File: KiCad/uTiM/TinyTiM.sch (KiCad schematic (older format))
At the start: 6 parts, among them P1 Data_In_Serial, P2 Data_Out_Serial, P5 Data_In_Serial, P6 Data_Out_Serial

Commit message: microTiM aka uTiM work in progress
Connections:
- net DI_A: now also P5.3 (P3); no longer P5.1 (P1)
- net GND: now also P5.1 (P1); no longer P5.3 (P3)
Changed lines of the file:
@@
 01 31 04 0B 88 21 58 40 0C C1 02 62 08 16 10 43 B0 80 18 82 05 C4 10 2C 20 86 60 01 31 04 0B 88
 21 58 40 0C C1 02 62 08 16 10 43 B0 80 18 82 05 C4 10 2C 20 86 60 01 31 04 0B 88 21 58 40 0C C1
-02 62 7C 03 3D 79 5E 0E 30 13 47 E7 00 00 00 00 49 45 4E 44 AE 42 60 82 81
+02 62 7C 03 3D 79 5E 0E 30 13 47 E7 00 00 00 00 49 45 4E 44 AE 42 60 82 E0
 EndData
 $EndBitmap
@@
 C1 ED 35 72 E0 F7 FB FF F1 1F FF F1 9F FF F9 9F C7 C7 C7 73 1A 9F 2B 70 38 1C FB F6 ED 3B 79 F2
 E4 23 8F 3C 52 B0 F1 D9 2E 76 F1 FF 03 17 ED 19 47 28 92 59 FB 00 00 00 00 49 45 4E 44 AE 42 60
-82 3D
+82 6C
 EndData
 $EndBitmap
@@
 F2 "GND" I L 8000 2000 60
 F3 "5V" I R 10050 2000 60
-F4 "DO_G" O R 10050 1700 60
+F4 "DI_H" O R 10050 1700 60
 F5 "DI_G" I L 8000 1700 60
-F6 "CO_G" O R 10050 1850 60
+F6 "CI_H" O R 10050 1850 60
 F7 "CI_G" I L 8000 1850 60
 $EndSheet
@@
 F2 "GND" I L 8000 2750 60
 F3 "5V" I R 10050 2750 60
-F4 "DO_F" O R 10050 2450 60
+F4 "DI_G" O R 10050 2450 60
 F5 "DI_F" I L 8000 2450 60
-F6 "CO_F" O R 10050 2600 60
+F6 "CI_G" O R 10050 2600 60
 F7 "CI_F" I L 8000 2600 60
 $EndSheet
@@
 F2 "GND" I L 8000 3500 60
 F3 "5V" I R 10050 3500 60
-F4 "DO_E" O R 10050 3200 60
+F4 "DI_F" O R 10050 3200 60
 F5 "DI_E" I L 8000 3200 60
-F6 "CO_E" O R 10050 3350 60
+F6 "CI_F" O R 10050 3350 60
 F7 "CI_E" I L 8000 3350 60
 $EndSheet
@@
 F2 "GND" I L 8000 4250 60
 F3 "5V" I R 10050 4250 60
-F4 "DO_D" O R 10050 3950 60
-F5 "DI_D" I L 8000 3950 60
-F6 "CO_D" O R 10050 4100 60
-F7 "CI_D" I L 8000 4100 60
+F4 "DI_D" I L 8000 3950 60
+F5 "CI_D" I L 8000 4100 60
+F6 "CI_E" O R 10050 4100 60
+F7 "DI_E" O R 10050 3950 60
 $EndSheet
 $Sheet
@@
 F2 "GND" I L 8000 5000 60
 F3 "5V" I R 10050 5000 60
-F4 "DO_C" O R 10050 4700 60
-F5 "DI_C" I L 8000 4700 60
-F6 "CO_C" O R 10050 4850 60
-F7 "CI_C" I L 8000 4850 60
+F4 "DI_C" I L 8000 4700 60
+F5 "CI_C" I L 8000 4850 60
+F6 "CI_D" O R 10050 4850 60
+F7 "DI_D" O R 10050 4700 60
 $EndSheet
 $Sheet
@@
 F2 "GND" I L 8000 5750 60
 F3 "5V" I R 10050 5750 60
-F4 "DO_B" O R 10050 5450 60
-F5 "DI_B" I L 8000 5450 60
-F6 "CO_B" O R 10050 5600 60
-F7 "CI_B" I L 8000 5600 60
+F4 "DI_B" I L 8000 5450 60
+F5 "CI_B" I L 8000 5600 60
+F6 "CI_C" O R 10050 5600 60
+F7 "DI_C" O R 10050 5450 60
 $EndSheet
 $Sheet
@@
 F0 "Row_A" 40
 F1 "Row_A.sch" 40
-F2 "DO_A" O R 10050 6200 60
-F3 "GND" I L 8000 6500 60
-F4 "DI_A" I L 8000 6200 60
-F5 "5V" I R 10050 6500 60
-F6 "CO_A" O R 10050 6350 60
-F7 "CI_A" I L 8000 6350 60
+F2 "GND" I L 8000 6500 60
+F3 "DI_A" I L 8000 6200 60
+F4 "5V" I R 10050 6500 60
+F5 "CI_A" I L 8000 6350 60
+F6 "CI_B" O R 10050 6350 60
+F7 "DI_B" O R 10050 6200 60
 $EndSheet
 $Comp
@@
 Text Label 10600 2000 2    60   ~ 0
 5V
-Text Label 10600 1700 2    60   ~ 0
-DO_G
 Wire Wire Line
 	10600 2000 10050 2000
 Wire Wire Line
 	10600 1850 10050 1850
-Text Label 10600 1850 2    60   ~ 0
-CO_G
 Wire Wire Line
 	10050 2450 10600 2450
 Text Label 10600 2750 2    60   ~ 0
 5V
-Text Label 10600 2450 2    60   ~ 0
-DO_F
 Wire Wire Line
 	10600 2750 10050 2750
 Wire Wire Line
 	10600 2600 10050 2600
-Text Label 10600 2600 2    60   ~ 0
-CO_F
 Wire Wire Line
 	10050 3200 10600 3200
 Text Label 10600 3500 2    60   ~ 0
 5V
-Text Label 10600 3200 2    60   ~ 0
-DO_E
 Wire Wire Line
 	10600 3500 10050 3500
 Wire Wire Line
 	10600 3350 10050 3350
-Text Label 10600 3350 2    60   ~ 0
-CO_E
 Wire Wire Line
 	10050 3950 10600 3950
 Text Label 10600 4250 2    60   ~ 0
 5V
-Text Label 10600 3950 2    60   ~ 0
-DO_D
 Wire Wire Line
 	10600 4250 10050 4250
 Wire Wire Line
 	10600 4100 10050 4100
-Text Label 10600 4100 2    60   ~ 0
-CO_D
 Wire Wire Line
 	10050 4700 10600 4700
 Text Label 10600 5000 2    60   ~ 0
 5V
-Text Label 10600 4700 2    60   ~ 0
-DO_C
 Wire Wire Line
 	10600 5000 10050 5000
 Wire Wire Line
 	10600 4850 10050 4850
-Text Label 10600 4850 2    60   ~ 0
-CO_C
 Wire Wire Line
 	10050 5450 10600 5450
@@
 5V
 Text Label 10600 5450 2    60   ~ 0
-DO_B
+DI_C
 Wire Wire Line
 	10600 5750 10050 5750
@@
 	10600 5600 10050 5600
 Text Label 10600 5600 2    60   ~ 0
-CO_B
+CI_C
 Wire Wire Line
 	10050 6200 10600 6200
 Text Label 10600 6500 2    60   ~ 0
 5V
-Text Label 10600 6200 2    60   ~ 0
-DO_A
 Wire Wire Line
 	10600 6500 10050 6500
 Wire Wire Line
 	10600 6350 10050 6350
-Text Label 10600 6350 2    60   ~ 0
-CO_A
 Wire Wire Line
 	2800 1450 3050 1450
@@
 F 6 "0.1\"" H 1350 2575 60  0001 L CNN "Field6"
 	1    1350 2325
-	-1   0    0    -1
+	-1   0    0    1
 $EndComp
 $Comp
@@
 	1    0    0    -1
 $EndComp
+Text Label 10600 6200 2    60   ~ 0
+DI_B
+Text Label 10600 6350 2    60   ~ 0
+CI_B
+Text Label 10600 4700 2    60   ~ 0
+DI_D
+Text Label 10600 4850 2    60   ~ 0
+CI_D
+Text Label 10600 3950 2    60   ~ 0
+DI_E
+Text Label 10600 4100 2    60   ~ 0
+CI_E
+Text Label 10600 3200 2    60   ~ 0
+DI_F
+Text Label 10600 3350 2    60   ~ 0
+CI_F
+Text Label 10600 2450 2    60   ~ 0
+DI_G
+Text Label 10600 2600 2    60   ~ 0
+CI_G
+Text Label 10600 1700 2    60   ~ 0
+DI_H
+Text Label 10600 1850 2    60   ~ 0
+CI_H
 $EndSCHEMATC

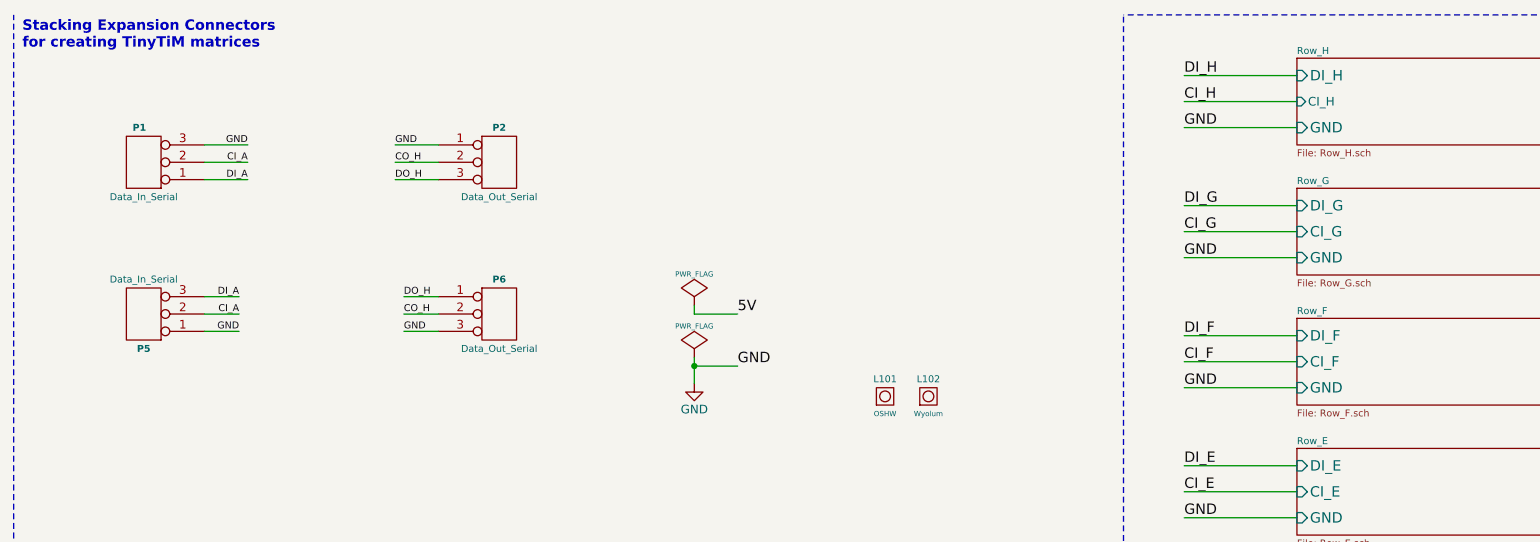
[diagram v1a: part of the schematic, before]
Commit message: work in progress, microTIM using APA102
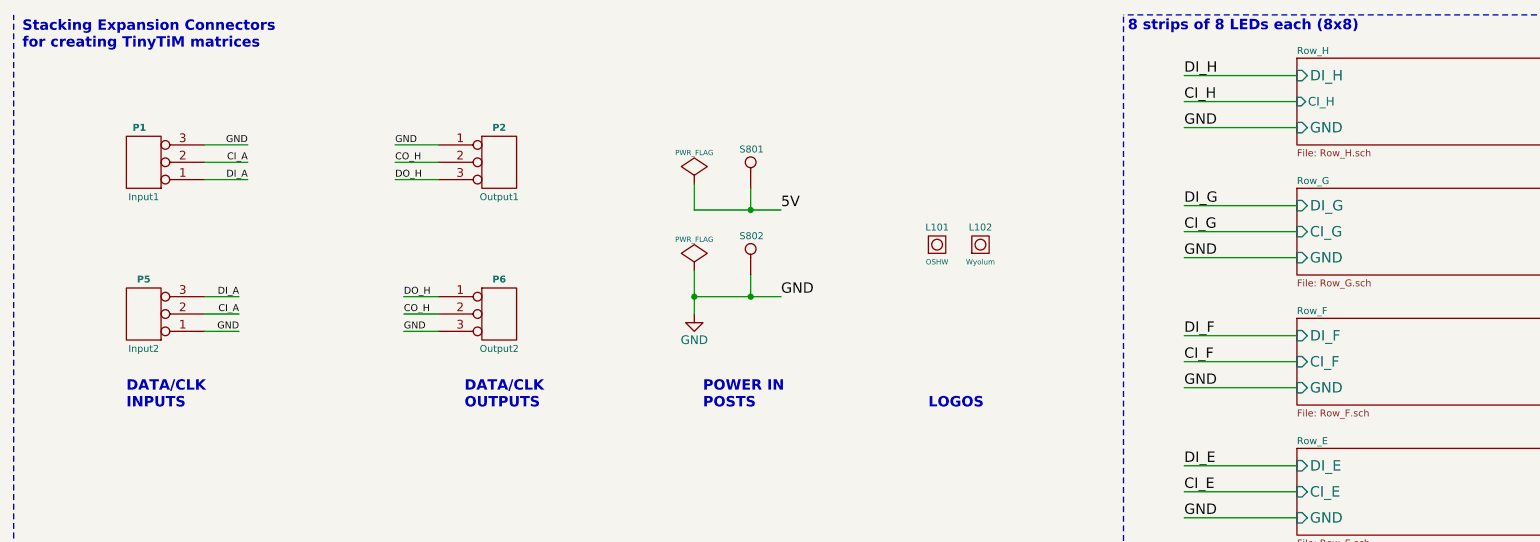
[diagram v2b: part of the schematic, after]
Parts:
- added S801: 5V, symbol CONN_1
- added S802: GND, symbol CONN_1
- P1: value Data_In_Serial -> Input1; footprint TinyTiM_Libs:Conn_x3_PTSM -> TinyTiM_Libs:JST_3pin_SRSS
- P2: value Data_Out_Serial -> Output1; footprint TinyTiM_Libs:Conn_x3_PTSM -> TinyTiM_Libs:JST_3pin_SRSS
- P5: value Data_In_Serial -> Input2; footprint TinyTiM_Libs:Conn_x3_PTSM -> TinyTiM_Libs:JST_3pin_SRSS
- P6: value Data_Out_Serial -> Output2; footprint TinyTiM_Libs:Conn_x3_PTSM -> TinyTiM_Libs:JST_3pin_SRSS
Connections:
- net 5V: now also S801.1
- net GND: now also S802.1
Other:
- note added: "8 strips of 8 LEDs each (8x8)"
- note added: "DATA/CLK\nINPUTS"
- note added: "DATA/CLK\nOUTPUTS"
- note added: "LOGOS"
- note added: "POWER IN\nPOSTS"
- moved on the sheet: L101, L102
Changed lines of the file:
@@
 01 31 04 0B 88 21 58 40 0C C1 02 62 08 16 10 43 B0 80 18 82 05 C4 10 2C 20 86 60 01 31 04 0B 88
 21 58 40 0C C1 02 62 08 16 10 43 B0 80 18 82 05 C4 10 2C 20 86 60 01 31 04 0B 88 21 58 40 0C C1
-02 62 7C 03 3D 79 5E 0E 30 13 47 E7 00 00 00 00 49 45 4E 44 AE 42 60 82 E0
+02 62 7C 03 3D 79 5E 0E 30 13 47 E7 00 00 00 00 49 45 4E 44 AE 42 60 82 31
 EndData
 $EndBitmap
@@
 C1 ED 35 72 E0 F7 FB FF F1 1F FF F1 9F FF F9 9F C7 C7 C7 73 1A 9F 2B 70 38 1C FB F6 ED 3B 79 F2
 E4 23 8F 3C 52 B0 F1 D9 2E 76 F1 FF 03 17 ED 19 47 28 92 59 FB 00 00 00 00 49 45 4E 44 AE 42 60
-82 6C
+82 3D
 EndData
 $EndBitmap
@@
 	10050 950  10600 950
 Wire Wire Line
-	4525 2325 4775 2325
-Wire Wire Line
-	4525 2275 4525 2325
+	4525 1725 5025 1725
+Wire Wire Line
+	4525 1575 4525 1725
 Wire Wire Line
 	1700 1350 1950 1350
@@
 L LOGO_1 L101
 U 1 1 511CD9F8
-P 5625 2800
-F 0 "L101" V 5725 2800 40  0000 C CNN
-F 1 "OSHW" V 5525 2800 30  0000 C CNN
-F 2 "TinyTiM_Lib:OSHW_6mm" H 5625 2955 30  0001 C CNN
-F 3 "" H 5625 2800 60  0001 C CNN
-	1    5625 2800
+P 5925 1925
+F 0 "L101" V 6025 1925 40  0000 C CNN
+F 1 "OSHW" V 5825 1925 30  0000 C CNN
+F 2 "TinyTiM_Lib:OSHW_6mm" H 5925 2080 30  0001 C CNN
+F 3 "" H 5925 1925 60  0001 C CNN
+	1    5925 1925
 	0    -1   -1   0
 $EndComp
@@
 L LOGO_1 L102
 U 1 1 511CD9F5
-P 5875 2800
-F 0 "L102" V 5975 2800 40  0000 C CNN
-F 1 "Wyolum" V 5775 2800 30  0000 C CNN
-F 2 "TinyTiM_Lib:Logo-WL3" H 5800 2875 30  0001 C CNN
-F 3 "" H 5875 2800 60  0001 C CNN
-	1    5875 2800
+P 6175 1925
+F 0 "L102" V 6275 1925 40  0000 C CNN
+F 1 "Wyolum" V 6075 1925 30  0000 C CNN
+F 2 "TinyTiM_Lib:Logo-WL3" H 6100 2000 30  0001 C CNN
+F 3 "" H 6175 1925 60  0001 C CNN
+	1    6175 1925
 	0    -1   -1   0
 $EndComp
@@
 L PWR_FLAG #FLG01
 U 1 1 50E7FAAF
-P 4525 2275
-F 0 "#FLG01" H 4525 2370 30  0001 C CNN
-F 1 "PWR_FLAG" H 4525 2455 30  0000 C CNN
-F 2 "" H 4525 2275 60  0001 C CNN
-F 3 "" H 4525 2275 60  0001 C CNN
-	1    4525 2275
+P 4525 1575
+F 0 "#FLG01" H 4525 1670 30  0001 C CNN
+F 1 "PWR_FLAG" H 4525 1755 30  0000 C CNN
+F 2 "" H 4525 1575 60  0001 C CNN
+F 3 "" H 4525 1575 60  0001 C CNN
+	1    4525 1575
 	1    0    0    -1
 $EndComp
-Text Label 4775 2325 0    60   ~ 0
+Text Label 5025 1725 0    60   ~ 0
 5V
 Text Label 1900 2225 2    40   ~ 0
@@
 CI_A
 Wire Wire Line
-	4775 2625 4525 2625
-Wire Wire Line
-	4525 2575 4525 2725
+	5025 2225 4525 2225
+Wire Wire Line
+	4525 2075 4525 2325
 $Comp
 L GND #PWR02
 U 1 1 56C3FF09
-P 4525 2725
-F 0 "#PWR02" H 4525 2475 50  0001 C CNN
-F 1 "GND" H 4525 2575 50  0000 C CNN
-F 2 "" H 4525 2725 50  0000 C CNN
-F 3 "" H 4525 2725 50  0000 C CNN
-	1    4525 2725
+P 4525 2325
+F 0 "#PWR02" H 4525 2075 50  0001 C CNN
+F 1 "GND" H 4525 2175 50  0000 C CNN
+F 2 "" H 4525 2325 50  0000 C CNN
+F 3 "" H 4525 2325 50  0000 C CNN
+	1    4525 2325
 	1    0    0    -1
 $EndComp
-Text Label 4775 2625 0    60   ~ 0
+Text Label 5025 2225 0    60   ~ 0
 GND
 $Comp
 L PWR_FLAG #FLG03
 U 1 1 56C40925
-P 4525 2575
-F 0 "#FLG03" H 4525 2670 30  0001 C CNN
-F 1 "PWR_FLAG" H 4525 2755 30  0000 C CNN
-F 2 "" H 4525 2575 60  0001 C CNN
-F 3 "" H 4525 2575 60  0001 C CNN
-	1    4525 2575
+P 4525 2075
+F 0 "#FLG03" H 4525 2170 30  0001 C CNN
+F 1 "PWR_FLAG" H 4525 2255 30  0000 C CNN
+F 2 "" H 4525 2075 60  0001 C CNN
+F 3 "" H 4525 2075 60  0001 C CNN
+	1    4525 2075
 	1    0    0    -1
 $EndComp
-Connection ~ 4525 2625
+Connection ~ 4525 2225
 $Comp
 L CONN_3 P1
@@
 P 1350 1450
 F 0 "P1" H 1375 1250 40  0000 C CNB
-F 1 "Data_In_Serial" H 1350 1650 40  0000 C CNN
-F 2 "TinyTiM_Libs:Conn_x3_PTSM" H 1350 1400 60  0001 C CNN
+F 1 "Input1" H 1350 1650 40  0000 C CNN
+F 2 "TinyTiM_Libs:JST_3pin_SRSS" H 1350 1400 60  0001 C CNN
 F 3 "" H 1350 1400 60  0000 C CNN
 F 4 "CONN HEADER 50POS .100\" SGL GOLD" H 1350 1500 60  0001 L CNN "Field4"
@@
 P 3400 1450
 F 0 "P2" H 3400 1650 40  0000 C CNB
-F 1 "Data_Out_Serial" H 3400 1250 40  0000 C CNN
-F 2 "TinyTiM_Libs:Conn_x3_PTSM" H 3400 1400 60  0001 C CNN
+F 1 "Output1" H 3400 1250 40  0000 C CNN
+F 2 "TinyTiM_Libs:JST_3pin_SRSS" H 3400 1400 60  0001 C CNN
 F 3 "" H 3400 1400 60  0000 C CNN
 F 4 "CONN HEADER 50POS .100\" SGL GOLD" H 3400 1500 60  0001 L CNN "Field4"
@@
 U 1 1 56C10A4A
 P 1350 2325
-F 0 "P5" H 1350 2525 40  0000 C CNB
-F 1 "Data_In_Serial" H 1350 2125 40  0000 C CNN
-F 2 "TinyTiM_Libs:Conn_x3_PTSM" H 1350 2275 60  0001 C CNN
+F 0 "P5" H 1350 2125 40  0000 C CNB
+F 1 "Input2" H 1350 2525 40  0000 C CNN
+F 2 "TinyTiM_Libs:JST_3pin_SRSS" H 1350 2275 60  0001 C CNN
 F 3 "" H 1350 2275 60  0000 C CNN
 F 4 "CONN HEADER 50POS .100\" SGL GOLD" H 1350 2375 60  0001 L CNN "Field4"
@@
 P 3400 2325
 F 0 "P6" H 3400 2525 40  0000 C CNB
-F 1 "Data_Out_Serial" H 3400 2125 40  0000 C CNN
-F 2 "TinyTiM_Libs:Conn_x3_PTSM" H 3400 2275 60  0001 C CNN
+F 1 "Output2" H 3400 2125 40  0000 C CNN
+F 2 "TinyTiM_Libs:JST_3pin_SRSS" H 3400 2275 60  0001 C CNN
 F 3 "" H 3400 2275 60  0000 C CNN
 F 4 "CONN HEADER 50POS .100\" SGL GOLD" H 3400 2375 60  0001 L CNN "Field4"
@@
 Text Label 10600 1850 2    60   ~ 0
 CI_H
+$Comp
+L CONN_1 S801
+U 1 1 56C23A5D
+P 4850 1450
+F 0 "S801" V 4925 1375 40  0000 L CNN
+F 1 "5V" H 4850 1505 30  0001 C CNN
+F 2 "" H 4850 1450 60  0000 C CNN
+F 3 "" H 4850 1450 60  0000 C CNN
+F 4 "mfr_pn" H 4850 1450 60  0001 C CNN "manf#"
+	1    4850 1450
+	0    -1   -1   0
+$EndComp
+$Comp
+L CONN_1 S802
+U 1 1 56C2406F
+P 4850 1950
+F 0 "S802" V 4925 1875 40  0000 L CNN
+F 1 "GND" H 4850 2005 30  0001 C CNN
+F 2 "" H 4850 1950 60  0000 C CNN
+F 3 "" H 4850 1950 60  0000 C CNN
+F 4 "mfr_pn" H 4850 1950 60  0001 C CNN "manf#"
+	1    4850 1950
+	0    -1   -1   0
+$EndComp
+Wire Wire Line
+	4850 1600 4850 1725
+Connection ~ 4850 1725
+Wire Wire Line
+	4850 2100 4850 2225
+Connection ~ 4850 2225
+Text Notes 5875 2875 0    60   ~ 12
+LOGOS
+Text Notes 4575 2875 0    60   ~ 12
+POWER IN\nPOSTS
+Text Notes 3200 2875 0    60   ~ 12
+DATA/CLK\nOUTPUTS
+Text Notes 1250 2875 0    60   ~ 12
+DATA/CLK\nINPUTS
+Text Notes 7025 700  0    60   ~ 12
+8 strips of 8 LEDs each (8x8)
 $EndSCHEMATC

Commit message: microTiM aka uTiM work in progress
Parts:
- added L103: Maniacal Labs, TinyTiM_Libs:logo_MLlabs, symbol LOGO_1
- L102: footprint TinyTiM_Lib:Logo-WL3 -> TinyTiM_Libs:logo_wyo_butterfly
- P1, P2, P5, P6: footprint TinyTiM_Libs:JST_3pin_SRSS -> TinyTiM_Libs:header_3pos_smd_male
- S801, S802: footprint (none) -> TinyTiM_Libs:PowerIn_stud
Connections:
- net DI_A: now also P5.1 (P1); no longer P5.3 (P3)
- net DO_H: now also P6.3 (P3); no longer P6.1 (P1)
- net GND: now also P5.3 (P3), P6.1 (P1); no longer P5.1 (P1), P6.3 (P3)
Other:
- note removed: "CHANGES:\nReplaced 2 pin PWR IN connectors P1 , P2 \nwith 3 pin SERIAL_DATA_IN connectors\n\nThis allows shorter wiring when boards are stacked up \nas 2.5D Cube or 3D (transparent PCB) cube\n\nSerial Shorting Links are permanently linked for Serial Mode.\nCut the links for Parallel Mode\n\nUse screw holes for electrical connections (Serial)\nS101 = Data_In TOP Layer and Data_Out on BOT layer\nS1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"
- moved on the sheet: L101
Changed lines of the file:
@@
 01 31 04 0B 88 21 58 40 0C C1 02 62 08 16 10 43 B0 80 18 82 05 C4 10 2C 20 86 60 01 31 04 0B 88
 21 58 40 0C C1 02 62 08 16 10 43 B0 80 18 82 05 C4 10 2C 20 86 60 01 31 04 0B 88 21 58 40 0C C1
-02 62 7C 03 3D 79 5E 0E 30 13 47 E7 00 00 00 00 49 45 4E 44 AE 42 60 82 31
+02 62 7C 03 3D 79 5E 0E 30 13 47 E7 00 00 00 00 49 45 4E 44 AE 42 60 82 71
 EndData
 $EndBitmap
@@
 C1 ED 35 72 E0 F7 FB FF F1 1F FF F1 9F FF F9 9F C7 C7 C7 73 1A 9F 2B 70 38 1C FB F6 ED 3B 79 F2
 E4 23 8F 3C 52 B0 F1 D9 2E 76 F1 FF 03 17 ED 19 47 28 92 59 FB 00 00 00 00 49 45 4E 44 AE 42 60
-82 3D
+82 3C
 EndData
 $EndBitmap
-Wire Notes Line
-	600  4450 600  600
 Wire Wire Line
 	2800 1350 3050 1350
@@
 L LOGO_1 L101
 U 1 1 511CD9F8
-P 5925 1925
-F 0 "L101" V 6025 1925 40  0000 C CNN
-F 1 "OSHW" V 5825 1925 30  0000 C CNN
-F 2 "TinyTiM_Lib:OSHW_6mm" H 5925 2080 30  0001 C CNN
-F 3 "" H 5925 1925 60  0001 C CNN
-	1    5925 1925
+P 5825 1925
+F 0 "L101" V 5925 1925 40  0000 C CNN
+F 1 "OSHW" V 5725 1925 30  0000 C CNN
+F 2 "TinyTiM_Lib:OSHW_6mm" H 5825 2080 30  0001 C CNN
+F 3 "" H 5825 1925 60  0001 C CNN
+	1    5825 1925
 	0    -1   -1   0
 $EndComp
@@
 F 0 "L102" V 6275 1925 40  0000 C CNN
 F 1 "Wyolum" V 6075 1925 30  0000 C CNN
-F 2 "TinyTiM_Lib:Logo-WL3" H 6100 2000 30  0001 C CNN
+F 2 "TinyTiM_Libs:logo_wyo_butterfly" H 6100 2000 30  0001 C CNN
 F 3 "" H 6175 1925 60  0001 C CNN
 	1    6175 1925
@@
 Text Label 2800 1550 0    40   ~ 0
 DO_H
-Text Notes 650  7675 0    50   ~ 10
-CHANGES:\nReplaced 2 pin PWR IN connectors P1 , P2 \nwith 3 pin SERIAL_DATA_IN connectors\n\nThis allows shorter wiring when boards are stacked up \nas 2.5D Cube or 3D (transparent PCB) cube\n\nSerial Shorting Links are permanently linked for Serial Mode.\nCut the links for Parallel Mode\n\nUse screw holes for electrical connections (Serial)\nS101 = Data_In TOP Layer and Data_Out on BOT layer\nS102 = Data_In BOT Layer and Data_Out on TOP layer\nS801 = +5V on TOP and BOT Layers\nS802 = GND on TOP and BOT Layers
 Wire Wire Line
 	10600 1250 10050 1250
@@
 F 0 "P1" H 1375 1250 40  0000 C CNB
 F 1 "Input1" H 1350 1650 40  0000 C CNN
-F 2 "TinyTiM_Libs:JST_3pin_SRSS" H 1350 1400 60  0001 C CNN
+F 2 "TinyTiM_Libs:header_3pos_smd_male" H 1350 1400 60  0001 C CNN
 F 3 "" H 1350 1400 60  0000 C CNN
 F 4 "CONN HEADER 50POS .100\" SGL GOLD" H 1350 1500 60  0001 L CNN "Field4"
@@
 F 0 "P2" H 3400 1650 40  0000 C CNB
 F 1 "Output1" H 3400 1250 40  0000 C CNN
-F 2 "TinyTiM_Libs:JST_3pin_SRSS" H 3400 1400 60  0001 C CNN
+F 2 "TinyTiM_Libs:header_3pos_smd_male" H 3400 1400 60  0001 C CNN
 F 3 "" H 3400 1400 60  0000 C CNN
 F 4 "CONN HEADER 50POS .100\" SGL GOLD" H 3400 1500 60  0001 L CNN "Field4"
@@
 F 0 "P5" H 1350 2125 40  0000 C CNB
 F 1 "Input2" H 1350 2525 40  0000 C CNN
-F 2 "TinyTiM_Libs:JST_3pin_SRSS" H 1350 2275 60  0001 C CNN
+F 2 "TinyTiM_Libs:header_3pos_smd_male" H 1350 2275 60  0001 C CNN
 F 3 "" H 1350 2275 60  0000 C CNN
 F 4 "CONN HEADER 50POS .100\" SGL GOLD" H 1350 2375 60  0001 L CNN "Field4"
@@
 F 6 "0.1\"" H 1350 2575 60  0001 L CNN "Field6"
 	1    1350 2325
-	-1   0    0    1
+	-1   0    0    -1
 $EndComp
 $Comp
@@
 F 0 "P6" H 3400 2525 40  0000 C CNB
 F 1 "Output2" H 3400 2125 40  0000 C CNN
-F 2 "TinyTiM_Libs:JST_3pin_SRSS" H 3400 2275 60  0001 C CNN
+F 2 "TinyTiM_Libs:header_3pos_smd_male" H 3400 2275 60  0001 C CNN
 F 3 "" H 3400 2275 60  0000 C CNN
 F 4 "CONN HEADER 50POS .100\" SGL GOLD" H 3400 2375 60  0001 L CNN "Field4"
@@
 F 6 "0.1\"" H 3400 2575 60  0001 L CNN "Field6"
 	1    3400 2325
-	1    0    0    -1
+	1    0    0    1
 $EndComp
 Text Label 10600 6200 2    60   ~ 0
@@
 F 0 "S801" V 4925 1375 40  0000 L CNN
 F 1 "5V" H 4850 1505 30  0001 C CNN
-F 2 "" H 4850 1450 60  0000 C CNN
+F 2 "TinyTiM_Libs:PowerIn_stud" H 4850 1450 60  0001 C CNN
 F 3 "" H 4850 1450 60  0000 C CNN
 F 4 "mfr_pn" H 4850 1450 60  0001 C CNN "manf#"
@@
 F 0 "S802" V 4925 1875 40  0000 L CNN
 F 1 "GND" H 4850 2005 30  0001 C CNN
-F 2 "" H 4850 1950 60  0000 C CNN
+F 2 "TinyTiM_Libs:PowerIn_stud" H 4850 1950 60  0001 C CNN
 F 3 "" H 4850 1950 60  0000 C CNN
 F 4 "mfr_pn" H 4850 1950 60  0001 C CNN "manf#"
@@
 Text Notes 7025 700  0    60   ~ 12
 8 strips of 8 LEDs each (8x8)
+$Comp
+L LOGO_1 L103
+U 1 1 56C3209A
+P 6525 1925
+F 0 "L103" V 6625 1925 40  0000 C CNN
+F 1 "Maniacal Labs" V 6425 1925 30  0000 C CNN
+F 2 "TinyTiM_Libs:logo_MLlabs" H 6450 2000 30  0001 C CNN
+F 3 "" H 6525 1925 60  0001 C CNN
+	1    6525 1925
+	0    -1   -1   0
+$EndComp
 $EndSCHEMATC

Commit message: layout complete. Gerbers pending
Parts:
- renumbered S801 to P3, S802 to P4
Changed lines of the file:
@@
 C1 ED 35 72 E0 F7 FB FF F1 1F FF F1 9F FF F9 9F C7 C7 C7 73 1A 9F 2B 70 38 1C FB F6 ED 3B 79 F2
 E4 23 8F 3C 52 B0 F1 D9 2E 76 F1 FF 03 17 ED 19 47 28 92 59 FB 00 00 00 00 49 45 4E 44 AE 42 60
-82 3C
+82 71
 EndData
 $EndBitmap
@@
 CI_H
 $Comp
-L CONN_1 S801
+L CONN_1 P3
 U 1 1 56C23A5D
 P 4850 1450
-F 0 "S801" V 4925 1375 40  0000 L CNN
+F 0 "P3" V 4925 1375 40  0000 L CNB
 F 1 "5V" H 4850 1505 30  0001 C CNN
 F 2 "TinyTiM_Libs:PowerIn_stud" H 4850 1450 60  0001 C CNN
@@
 $EndComp
 $Comp
-L CONN_1 S802
+L CONN_1 P4
 U 1 1 56C2406F
 P 4850 1950
-F 0 "S802" V 4925 1875 40  0000 L CNN
+F 0 "P4" V 4925 1875 40  0000 L CNB
 F 1 "GND" H 4850 2005 30  0001 C CNN
 F 2 "TinyTiM_Libs:PowerIn_stud" H 4850 1950 60  0001 C CNN
